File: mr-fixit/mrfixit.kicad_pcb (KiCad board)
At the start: 2 copper layers, 69.3 x 99.8 mm, 3 parts, among them J1 Conn_02x03_Odd_Even

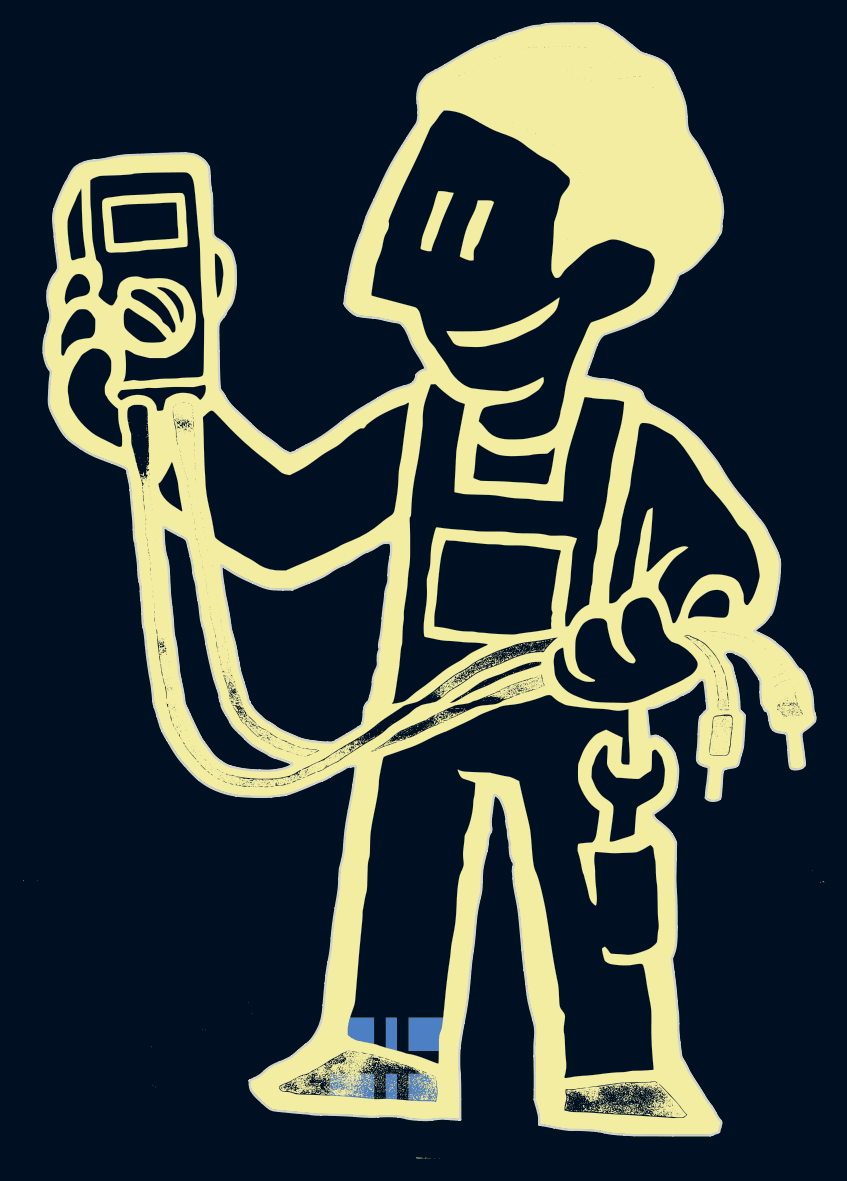
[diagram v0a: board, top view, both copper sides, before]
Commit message: mrfixit: v1.0 as submitted, hasl copper outline with red mask internal + multimeter led
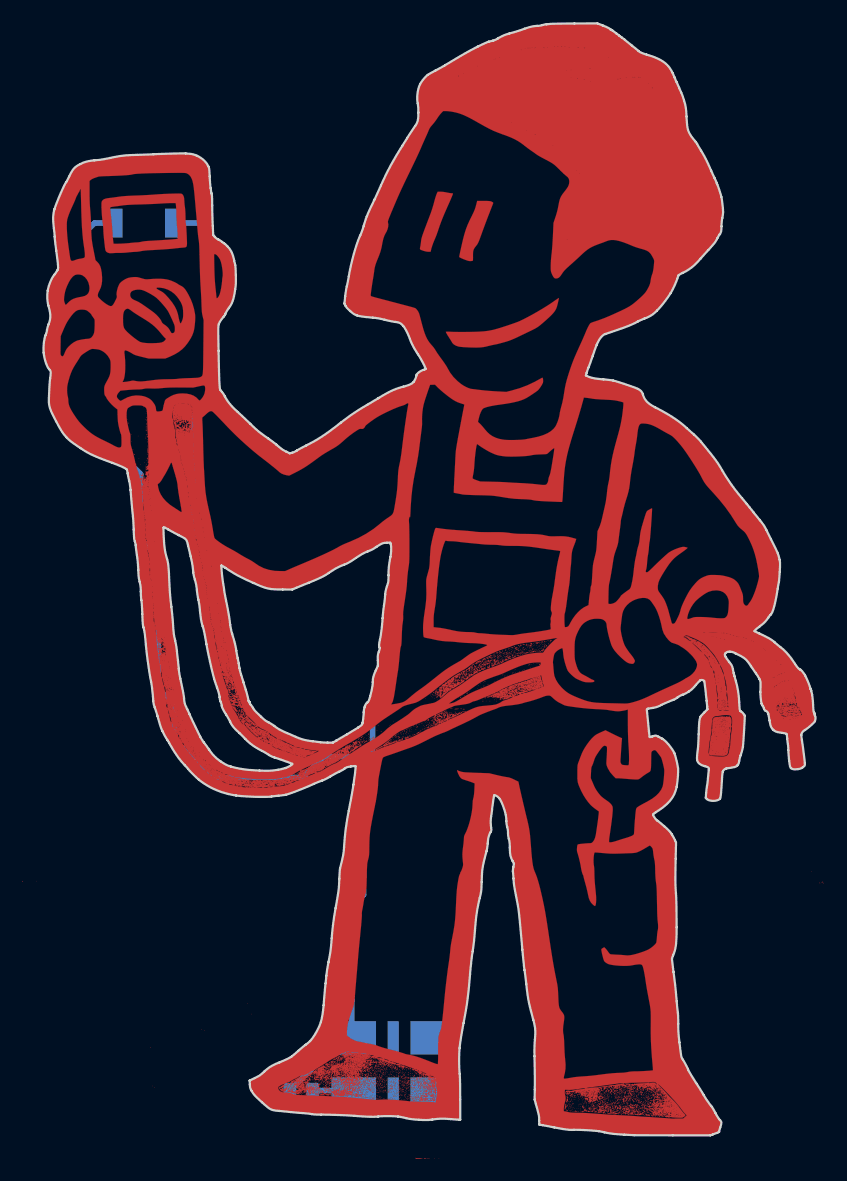
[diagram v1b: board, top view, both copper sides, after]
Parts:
- added D1: LED, tom-opto:XZM2CYK45WT-9-NOMASK, B.Cu at (106.7, 56.5)
- added R1: 220R, tom-passives:C_0805_2012Metric_Pad1.15x1.40mm_HandSolder, B.Cu at (120.8, 134.3)
- H1: footprint mr-fixit:mrfixit-mask-invert -> mr-fixit:mrfixit-mask
- H2: value Silk -> Copper; footprint mr-fixit:mrfixit-silk -> mr-fixit:mrfixit-copper
- moved J1 0.37 mm to (129.1, 132.1)
- moved H2 0.08 mm to (131.8, 88.8)
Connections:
- J1 pad 5: Net-(J1-Pad5) -> +3V3
- J1 pad 6: Net-(J1-Pad6) -> GND
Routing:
- net Net-(D1-Pad1): track 0.00 -> 106.8 mm
- net +3V3: track 0.00 -> 99.9 mm
- net GND: track 0.00 -> 3.81 mm
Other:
- board text added: "tom@tomk.in v1.0 @TomKeddie"

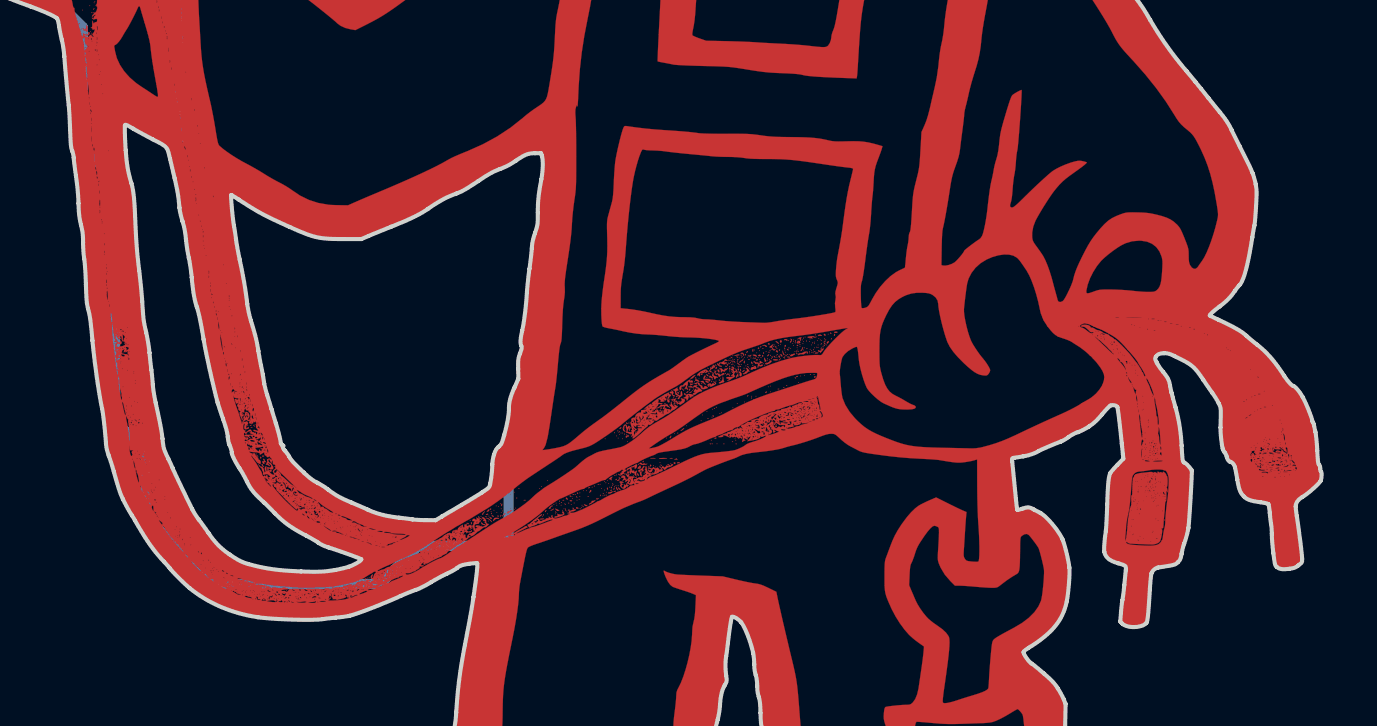
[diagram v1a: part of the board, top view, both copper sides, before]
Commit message: mr-fixit: v1.1 edge cuts changes as v1.0 failed audit
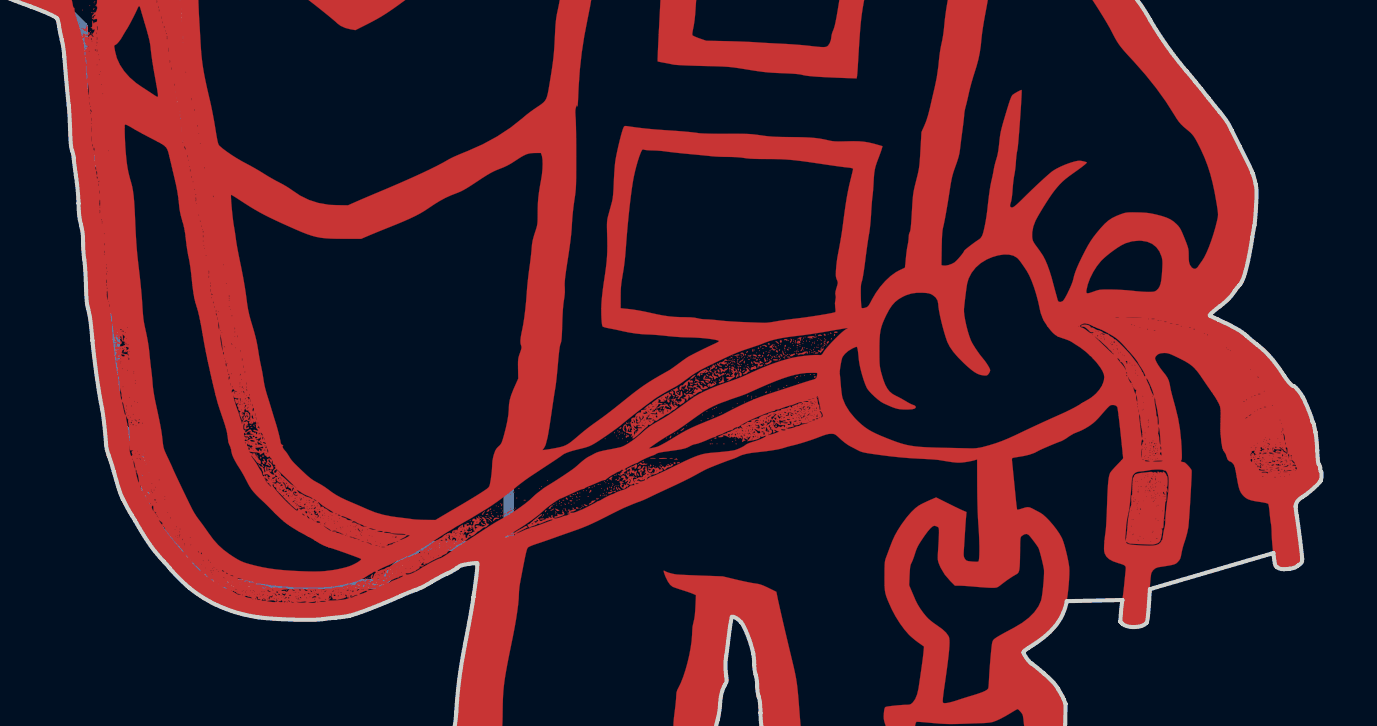
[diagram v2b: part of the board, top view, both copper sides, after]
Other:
- outline, holes or cut-outs redrawn
- board text added: "tom@tomk.in v1.1 @TomKeddie"
- board text removed: "tom@tomk.in v1.0 @TomKeddie"

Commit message: mrfixit: rev1.3 as sent for mfg
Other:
- net class Default removed
- board text added: "tom@tomk.in v1.3 Sep2025 @TomKeddie JLCJLCJLCJLC"
- board text removed: "tom@tomk.in v1.1 @TomKeddie"
